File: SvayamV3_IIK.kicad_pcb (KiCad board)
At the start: 2 copper layers, 169 parts, among them J1 USB_C_Receptacle_USB2.0_16P, J10 POWER2, J11 TELEM1, J12 TELEM2, J13 GPS, J14 SERIAL4, J15 SERIAL5, J16 I2C, J17 CAN, J18 BUZZER, J19 Conn_01x05_Pin, J2 Micro_SD_Card_Det1, J20 ADC, J21 SPI, J22 SAFETY, J23 CAN2, J24 SBUS, J3 S_TOP_SIG, J4 S_TOP_PWR, J5 S_TOP_GND, J6 S_SIDE_SIG, J7 S_SIDE_PWR, J8 S_SIDE_GND, J9 POWER1, Q1 AO3400A, SW1 TS-1010A-B, SW2 SK-3296S-01-L3, U1 STM32H743IIKx, U10 RT9080-33GJ5, U11 AP22804AW5, U12 USBLC6-2SC6, U13 TJA1051TK-3, U2 TJA1051TK-3, U3 FM25CL64B, U4 BMI088, U5 BMI270, U6 BMP388, U7 BMM150, U8 TPS2120YFPR, U9 RT9080-33GJ5, Y1 X50328MSB2GI

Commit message: Layout
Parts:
- added C46: 100n, Capacitor_SMD:C_0402_1005Metric, F.Cu at (171.0, 81.0)
- added C47: 4u7, Capacitor_SMD:C_0603_1608Metric, F.Cu at (171.6, 73.8)
- added C48: 4u7, Capacitor_SMD:C_0603_1608Metric, F.Cu at (171.6, 76.3)
- added C49: 100n, Capacitor_SMD:C_0402_1005Metric, F.Cu at (171.0, 83.0)
- added C50: 100n, Capacitor_SMD:C_0402_1005Metric, F.Cu at (171.0, 85.0)
- added C51: 10u, Capacitor_SMD:C_0603_1608Metric, F.Cu at (171.6, 78.8)
- added D6: SMAJ6.0A, Diode_SMD:D_SMA, F.Cu at (165.6, 74.8)
- added D7: SMAJ6.0A, Diode_SMD:D_SMA, F.Cu at (165.6, 79.3)
- added R75: 100k, Resistor_SMD:R_0402_1005Metric, F.Cu at (163.0, 82.6)
- added R76: 100k, Resistor_SMD:R_0402_1005Metric, F.Cu at (163.0, 84.6)
- J10, J11, J12, J13, J14, J15, J16, J17, J18, J22, J3, J4, J5, J6, J7, J8, J9: moved to B.Cu
- U1: value STM32H743IIKx -> STM32H743IIK6
- moved H4 127.0 mm to (150.3, 101.2)
- moved H2 114.2 mm to (150.3, 38.3)
- moved J11 106.3 mm to (137.9, 42.6), turned to 180 degrees
- moved J13 106.0 mm to (139.0, 62.4), turned to 180 degrees
- moved J14 100.6 mm to (134.1, 72.5), turned to 180 degrees
- moved H3 95.7 mm to (107.3, 101.3)
- moved J12 93.8 mm to (121.4, 42.4), turned to 180 degrees
- moved J6 91.5 mm to (113.0, 95.5), turned to -90 degrees
- moved R28 89.4 mm to (142.0, 90.5)
- moved R41 89.0 mm to (135.9, 92.5), turned to -90 degrees
- moved R40 88.2 mm to (133.3, 92.5), turned to -90 degrees
- moved J15 87.8 mm to (118.1, 72.6), turned to 180 degrees
- moved R39 87.6 mm to (130.8, 92.5), turned to -90 degrees
- moved R38 87.0 mm to (128.2, 92.5), turned to -90 degrees
- moved R32 87.0 mm to (113.0, 92.4), turned to -90 degrees
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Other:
- board outline added: 51 x 70 mm
- copper layers 2 -> 6

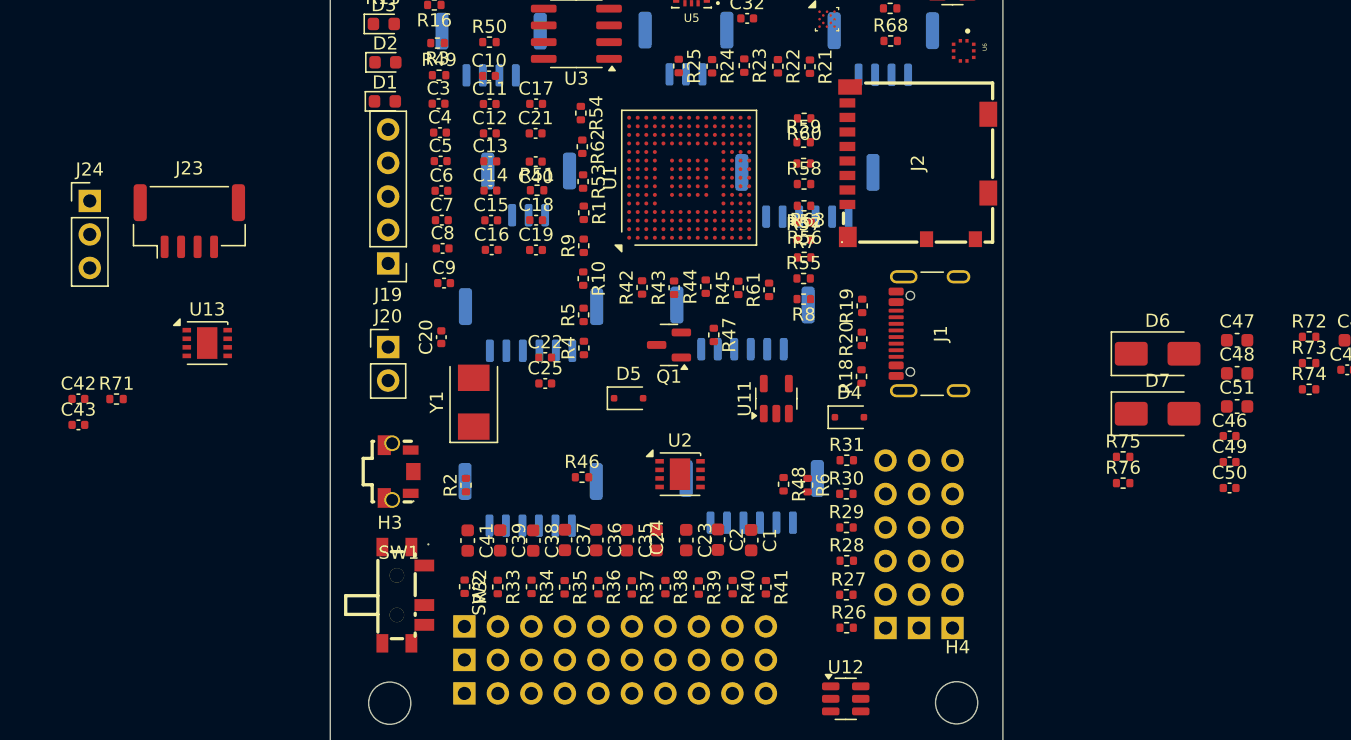
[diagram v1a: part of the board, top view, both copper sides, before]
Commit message: Schematic: sensor redundancy + blok current limiter GPS (terverifikasi)
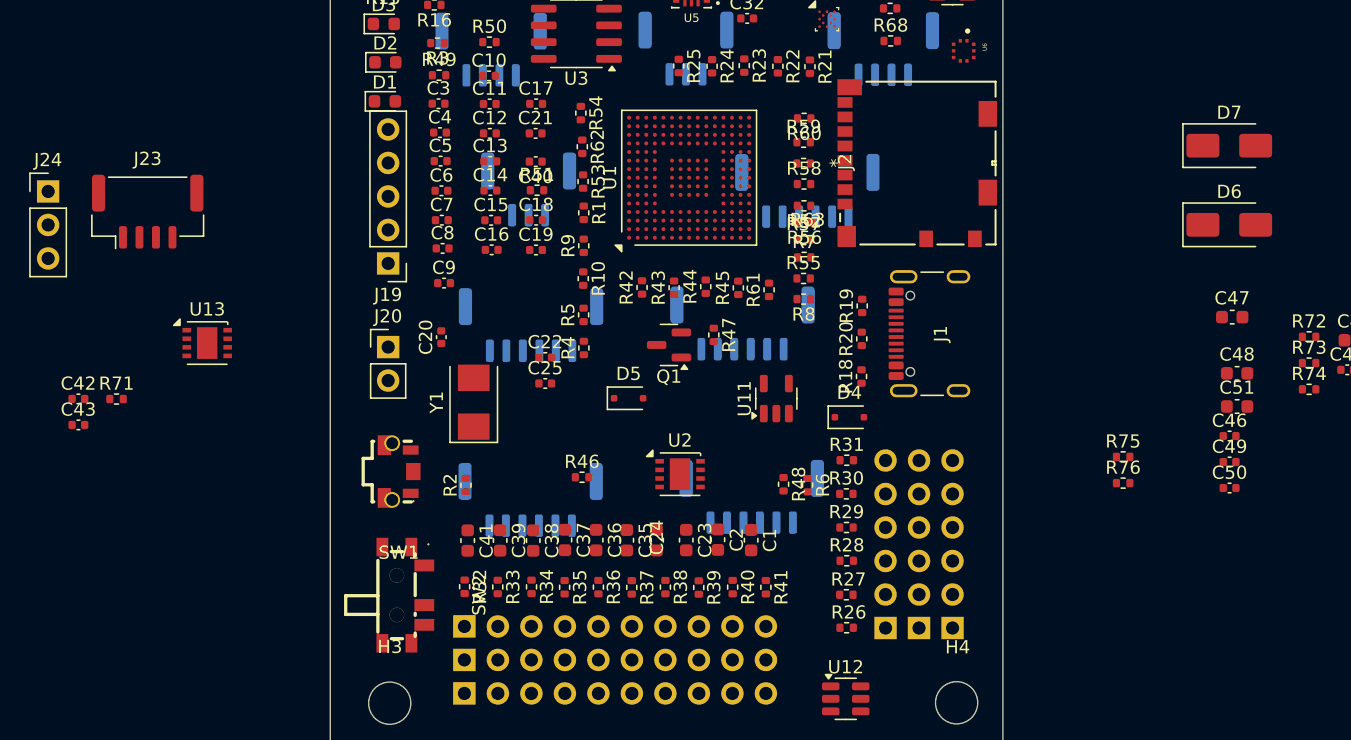
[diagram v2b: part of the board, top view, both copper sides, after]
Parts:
- J2: footprint easyeda2kicad:SIM-SMD_8P-1040310811 -> Svayam:104031-0811_MOL
- moved D7 21.0 mm to (171.0, 59.0)
- moved D6 11.2 mm to (171.0, 65.0)
- moved J23 3.24 mm to (89.0, 64.0)
- moved J24 3.24 mm to (81.5, 62.5)
- moved C47 1.79 mm to (171.2, 72.0)

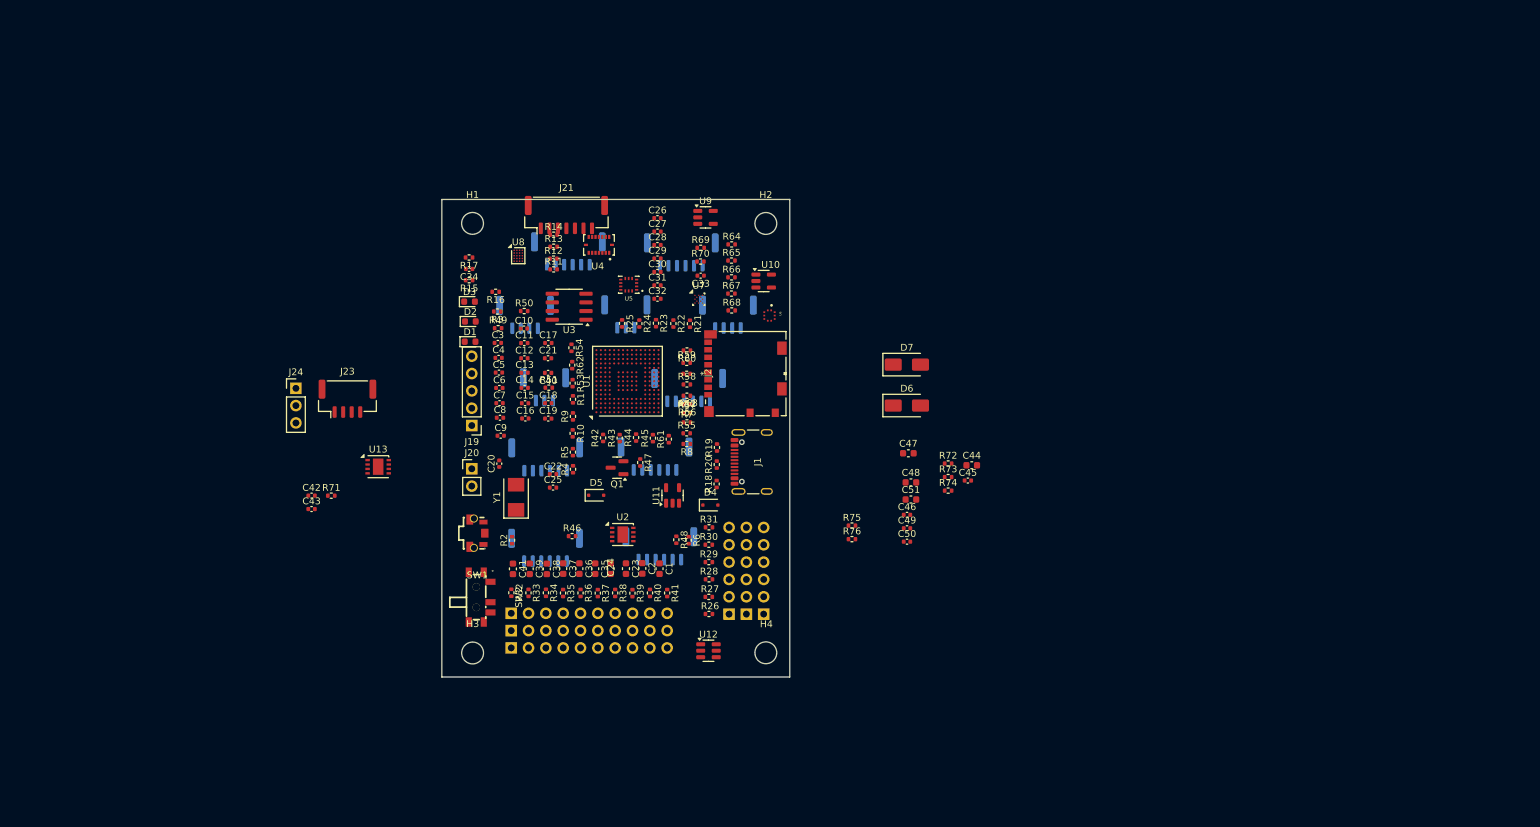
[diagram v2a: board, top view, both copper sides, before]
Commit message: PCB: F8 apply — 290 footprint di board (parity 0, verified)
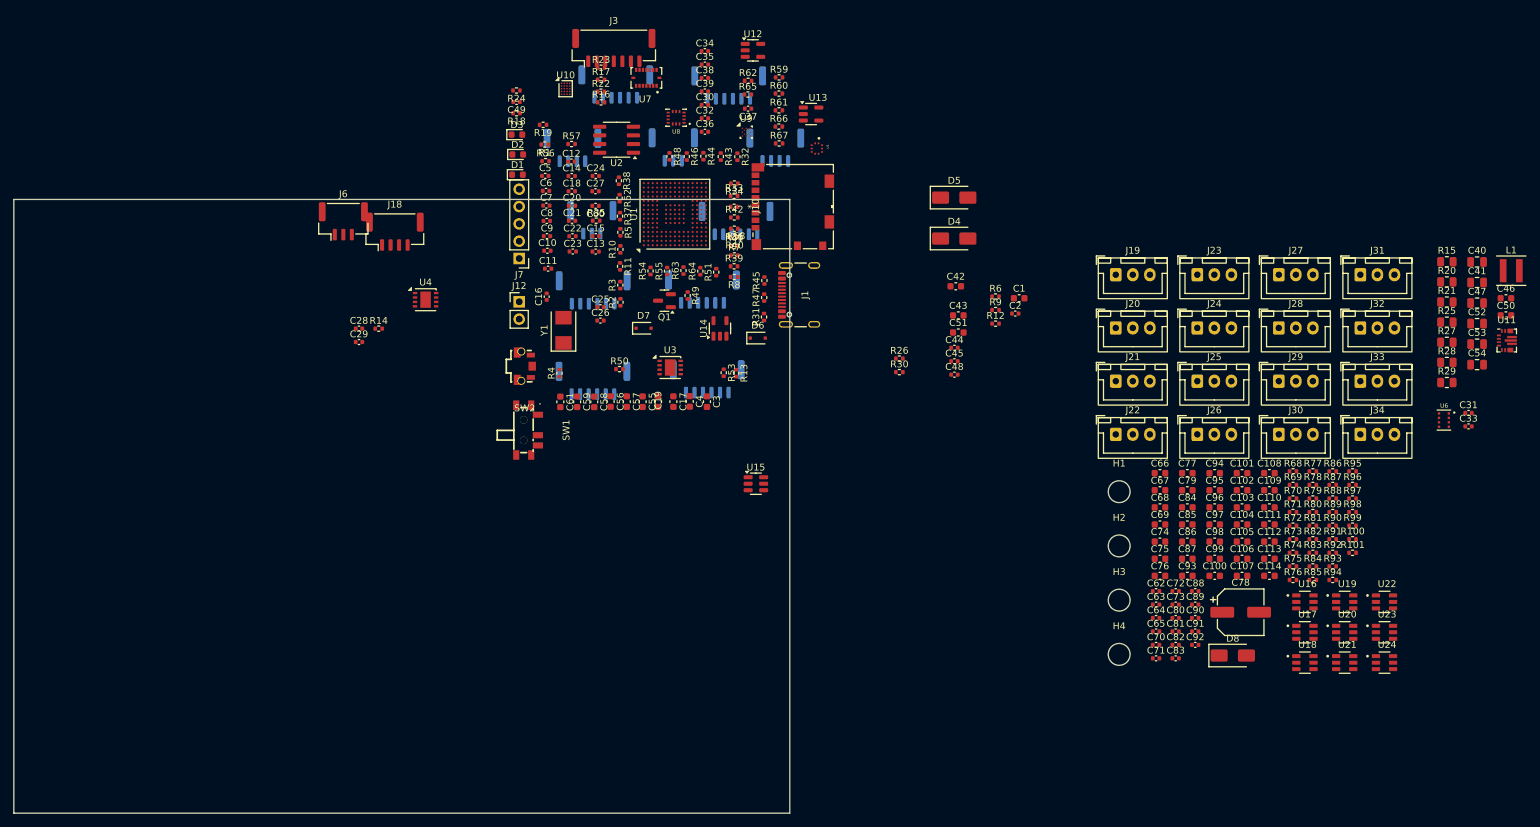
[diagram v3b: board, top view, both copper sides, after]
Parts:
- removed the J3 at (144.9, 95.6)
- removed the J4 at (147.5, 95.6)
- removed the J5 at (150.0, 95.6)
- removed the J6 at (113.0, 95.5)
- removed the J7 at (113.0, 98.0)
- removed the J8 at (113.0, 100.5)
- removed the R26 at (142.0, 95.5)
- removed the R30 at (142.0, 85.4)
- removed the R31 at (142.0, 82.8)
- removed the R32 at (113.0, 92.4)
- removed the R33 at (115.5, 92.5)
- removed the R34 at (118.1, 92.5)
- removed the R35 at (120.6, 92.5)
- removed the R36 at (123.2, 92.5)
- removed the R37 at (125.7, 92.5)
- removed the R38 at (128.2, 92.5)
- removed the R39 at (130.8, 92.5)
- removed the R40 at (133.3, 92.5)
- removed the R41 at (135.9, 92.5)
- added C100: 1u, Capacitor_SMD:C_0603_1608Metric, F.Cu at (216.1, 90.0)
- added C101: 1u, Capacitor_SMD:C_0603_1608Metric, F.Cu at (220.1, 74.9)
- added C102: 1u, Capacitor_SMD:C_0603_1608Metric, F.Cu at (220.1, 77.4)
- added C103: 1u, Capacitor_SMD:C_0603_1608Metric, F.Cu at (220.1, 79.9)
- added C104: 1u, Capacitor_SMD:C_0603_1608Metric, F.Cu at (220.1, 82.4)
- added C105: 1u, Capacitor_SMD:C_0603_1608Metric, F.Cu at (220.1, 84.9)
- added C106: 1u, Capacitor_SMD:C_0603_1608Metric, F.Cu at (220.1, 87.5)
- added C107: 1u, Capacitor_SMD:C_0603_1608Metric, F.Cu at (220.1, 90.0)
- added C108: 1u, Capacitor_SMD:C_0603_1608Metric, F.Cu at (224.1, 74.9)
- added C109: 1u, Capacitor_SMD:C_0603_1608Metric, F.Cu at (224.1, 77.4)
- added C110: 1u, Capacitor_SMD:C_0603_1608Metric, F.Cu at (224.1, 79.9)
- added C111: 1u, Capacitor_SMD:C_0603_1608Metric, F.Cu at (224.1, 82.4)
- added C112: 1u, Capacitor_SMD:C_0603_1608Metric, F.Cu at (224.1, 84.9)
- added C113: 1u, Capacitor_SMD:C_0603_1608Metric, F.Cu at (224.1, 87.5)
- added C114: 1u, Capacitor_SMD:C_0603_1608Metric, F.Cu at (224.1, 90.0)
- added C31: 100n, Capacitor_SMD:C_0402_1005Metric, F.Cu at (253.3, 66.1)
- added C33: 100n, Capacitor_SMD:C_0402_1005Metric, F.Cu at (253.3, 68.1)
- added C40: 10u, Capacitor_SMD:C_0805_2012Metric, F.Cu at (254.6, 44.0)
- added C41: 10u, Capacitor_SMD:C_0805_2012Metric, F.Cu at (254.6, 47.0)
- added C46: 10u, Capacitor_SMD:C_0603_1608Metric, F.Cu at (258.8, 49.3)
- added C47: 100n, Capacitor_SMD:C_0805_2012Metric, F.Cu at (254.6, 50.0)
- added C50: 10u, Capacitor_SMD:C_0603_1608Metric, F.Cu at (258.8, 51.8)
- added C52: 22u, Capacitor_SMD:C_0805_2012Metric, F.Cu at (254.6, 53.0)
- added C53: 22u, Capacitor_SMD:C_0805_2012Metric, F.Cu at (254.6, 56.0)
- added C54: 22u, Capacitor_SMD:C_0805_2012Metric, F.Cu at (254.6, 59.0)
- added C62: 100n, Capacitor_SMD:C_0402_1005Metric, F.Cu at (207.5, 92.2)
- added C63: 100n, Capacitor_SMD:C_0402_1005Metric, F.Cu at (207.5, 94.2)
- added C64: 100n, Capacitor_SMD:C_0402_1005Metric, F.Cu at (207.5, 96.1)
- added C65: 100n, Capacitor_SMD:C_0402_1005Metric, F.Cu at (207.5, 98.1)
- added C66: 1u, Capacitor_SMD:C_0603_1608Metric, F.Cu at (208.1, 74.9)
- added C67: 1u, Capacitor_SMD:C_0603_1608Metric, F.Cu at (208.1, 77.4)
- added C68: 1u, Capacitor_SMD:C_0603_1608Metric, F.Cu at (208.1, 79.9)
- added C69: 1u, Capacitor_SMD:C_0603_1608Metric, F.Cu at (208.1, 82.4)
- added C70: 100n, Capacitor_SMD:C_0402_1005Metric, F.Cu at (207.5, 100.1)
- added C71: 100n, Capacitor_SMD:C_0402_1005Metric, F.Cu at (207.5, 102.1)
- added C72: 100n, Capacitor_SMD:C_0402_1005Metric, F.Cu at (210.4, 92.2)
- added C73: 100n, Capacitor_SMD:C_0402_1005Metric, F.Cu at (210.4, 94.2)
- added C74: 1u, Capacitor_SMD:C_0603_1608Metric, F.Cu at (208.1, 84.9)
- added C75: 1u, Capacitor_SMD:C_0603_1608Metric, F.Cu at (208.1, 87.5)
- added C76: 1u, Capacitor_SMD:C_0603_1608Metric, F.Cu at (208.1, 90.0)
- added C77: 1u, Capacitor_SMD:C_0603_1608Metric, F.Cu at (212.1, 74.9)
- added C78: 220u, Capacitor_SMD:CP_Elec_6.3x7.7, F.Cu at (219.9, 95.3)
- added C79: 1u, Capacitor_SMD:C_0603_1608Metric, F.Cu at (212.1, 77.4)
- added C80: 100n, Capacitor_SMD:C_0402_1005Metric, F.Cu at (210.4, 96.1)
- added C81: 100n, Capacitor_SMD:C_0402_1005Metric, F.Cu at (210.4, 98.1)
- added C82: 100n, Capacitor_SMD:C_0402_1005Metric, F.Cu at (210.4, 100.1)
- added C83: 100n, Capacitor_SMD:C_0402_1005Metric, F.Cu at (210.4, 102.1)
- added C84: 1u, Capacitor_SMD:C_0603_1608Metric, F.Cu at (212.1, 79.9)
- added C85: 1u, Capacitor_SMD:C_0603_1608Metric, F.Cu at (212.1, 82.4)
- added C86: 1u, Capacitor_SMD:C_0603_1608Metric, F.Cu at (212.1, 84.9)
- added C87: 1u, Capacitor_SMD:C_0603_1608Metric, F.Cu at (212.1, 87.5)
- added C88: 100n, Capacitor_SMD:C_0402_1005Metric, F.Cu at (213.3, 92.2)
- added C89: 100n, Capacitor_SMD:C_0402_1005Metric, F.Cu at (213.3, 94.2)
- added C90: 100n, Capacitor_SMD:C_0402_1005Metric, F.Cu at (213.3, 96.1)
- added C91: 100n, Capacitor_SMD:C_0402_1005Metric, F.Cu at (213.3, 98.1)
- added C92: 100n, Capacitor_SMD:C_0402_1005Metric, F.Cu at (213.3, 100.1)
- added C93: 1u, Capacitor_SMD:C_0603_1608Metric, F.Cu at (212.1, 90.0)
- added C94: 1u, Capacitor_SMD:C_0603_1608Metric, F.Cu at (216.1, 74.9)
- added C95: 1u, Capacitor_SMD:C_0603_1608Metric, F.Cu at (216.1, 77.4)
- added C96: 1u, Capacitor_SMD:C_0603_1608Metric, F.Cu at (216.1, 79.9)
- added C97: 1u, Capacitor_SMD:C_0603_1608Metric, F.Cu at (216.1, 82.4)
- added C98: 1u, Capacitor_SMD:C_0603_1608Metric, F.Cu at (216.1, 84.9)
- added C99: 1u, Capacitor_SMD:C_0603_1608Metric, F.Cu at (216.1, 87.5)
- added D8: SMAJ6.0A, Diode_SMD:D_SMA, F.Cu at (218.8, 101.6)
- added J19: Channel 1, Connector_JST:JST_XH_B3B-XH-A_1x03_P2.50mm_Vertical, F.Cu at (201.6, 45.8)
- added J20: Channel 5, Connector_JST:JST_XH_B3B-XH-A_1x03_P2.50mm_Vertical, F.Cu at (201.6, 53.6)
- added J21: Channel 9, Connector_JST:JST_XH_B3B-XH-A_1x03_P2.50mm_Vertical, F.Cu at (201.6, 61.4)
- added J22: Channel 13, Connector_JST:JST_XH_B3B-XH-A_1x03_P2.50mm_Vertical, F.Cu at (201.6, 69.2)
- added J23: Channel 2, Connector_JST:JST_XH_B3B-XH-A_1x03_P2.50mm_Vertical, F.Cu at (213.6, 45.8)
- added J24: Channel 6, Connector_JST:JST_XH_B3B-XH-A_1x03_P2.50mm_Vertical, F.Cu at (213.6, 53.6)
- added J25: Channel 10, Connector_JST:JST_XH_B3B-XH-A_1x03_P2.50mm_Vertical, F.Cu at (213.6, 61.4)
- added J26: Channel 14, Connector_JST:JST_XH_B3B-XH-A_1x03_P2.50mm_Vertical, F.Cu at (213.6, 69.2)
- added J27: Channel 3, Connector_JST:JST_XH_B3B-XH-A_1x03_P2.50mm_Vertical, F.Cu at (225.5, 45.8)
- added J28: Channel 7, Connector_JST:JST_XH_B3B-XH-A_1x03_P2.50mm_Vertical, F.Cu at (225.5, 53.6)
- added J29: Channel 11, Connector_JST:JST_XH_B3B-XH-A_1x03_P2.50mm_Vertical, F.Cu at (225.5, 61.4)
- added J30: Channel 15, Connector_JST:JST_XH_B3B-XH-A_1x03_P2.50mm_Vertical, F.Cu at (225.5, 69.2)
- added J31: Channel 4, Connector_JST:JST_XH_B3B-XH-A_1x03_P2.50mm_Vertical, F.Cu at (237.5, 45.8)
- added J32: Channel 8, Connector_JST:JST_XH_B3B-XH-A_1x03_P2.50mm_Vertical, F.Cu at (237.5, 53.6)
- added J33: Channel 12, Connector_JST:JST_XH_B3B-XH-A_1x03_P2.50mm_Vertical, F.Cu at (237.5, 61.4)
- added J34: Channel 16, Connector_JST:JST_XH_B3B-XH-A_1x03_P2.50mm_Vertical, F.Cu at (237.5, 69.2)
- added L1: 1.5u, Svayam:L_Coilcraft_XxL4020, F.Cu at (259.6, 45.2)
- added R100: 10k, Resistor_SMD:R_0402_1005Metric, F.Cu at (236.3, 84.6)
- added R101: 10k, Resistor_SMD:R_0402_1005Metric, F.Cu at (236.3, 86.6)
- added R15: 10k, Resistor_SMD:R_0805_2012Metric, F.Cu at (250.2, 43.9)
- added R20: 100k, Resistor_SMD:R_0805_2012Metric, F.Cu at (250.2, 46.9)
- added R21: 10k, Resistor_SMD:R_0805_2012Metric, F.Cu at (250.2, 49.8)
- added R25: 100k, Resistor_SMD:R_0805_2012Metric, F.Cu at (250.2, 52.8)
- added R68: 120, Resistor_SMD:R_0402_1005Metric, F.Cu at (227.6, 74.6)
- added R69: 120, Resistor_SMD:R_0402_1005Metric, F.Cu at (227.6, 76.6)
- added R70: 120, Resistor_SMD:R_0402_1005Metric, F.Cu at (227.6, 78.6)
- added R71: 120, Resistor_SMD:R_0402_1005Metric, F.Cu at (227.6, 80.6)
- added R72: 120, Resistor_SMD:R_0402_1005Metric, F.Cu at (227.6, 82.6)
- added R73: 120, Resistor_SMD:R_0402_1005Metric, F.Cu at (227.6, 84.6)
- added R74: 120, Resistor_SMD:R_0402_1005Metric, F.Cu at (227.6, 86.6)
- added R75: 120, Resistor_SMD:R_0402_1005Metric, F.Cu at (227.6, 88.6)
- added R76: 120, Resistor_SMD:R_0402_1005Metric, F.Cu at (227.6, 90.6)
- added R77: 120, Resistor_SMD:R_0402_1005Metric, F.Cu at (230.5, 74.6)
- added R78: 120, Resistor_SMD:R_0402_1005Metric, F.Cu at (230.5, 76.6)
- added R79: 120, Resistor_SMD:R_0402_1005Metric, F.Cu at (230.5, 78.6)
- added R80: 120, Resistor_SMD:R_0402_1005Metric, F.Cu at (230.5, 80.6)
- added R81: 120, Resistor_SMD:R_0402_1005Metric, F.Cu at (230.5, 82.6)
- added R82: 120, Resistor_SMD:R_0402_1005Metric, F.Cu at (230.5, 84.6)
- added R83: 120, Resistor_SMD:R_0402_1005Metric, F.Cu at (230.5, 86.6)
- added R84: 33k, Resistor_SMD:R_0402_1005Metric, F.Cu at (230.5, 88.6)
- added R85: 33k, Resistor_SMD:R_0402_1005Metric, F.Cu at (230.5, 90.6)
- added R86: 75k, Resistor_SMD:R_0402_1005Metric, F.Cu at (233.4, 74.6)
- added R87: 75k, Resistor_SMD:R_0402_1005Metric, F.Cu at (233.4, 76.6)
- added R88: 110k, Resistor_SMD:R_0402_1005Metric, F.Cu at (233.4, 78.6)
- added R89: 47k, Resistor_SMD:R_0402_1005Metric, F.Cu at (233.4, 80.6)
- added R90: 56k, Resistor_SMD:R_0402_1005Metric, F.Cu at (233.4, 82.6)
- added R91: 110k, Resistor_SMD:R_0402_1005Metric, F.Cu at (233.4, 84.6)
- added R92: 47k, Resistor_SMD:R_0402_1005Metric, F.Cu at (233.4, 86.6)
- added R93: 10k, Resistor_SMD:R_0402_1005Metric, F.Cu at (233.4, 88.6)
- added R94: 10k, Resistor_SMD:R_0402_1005Metric, F.Cu at (233.4, 90.6)
- added R95: 10k, Resistor_SMD:R_0402_1005Metric, F.Cu at (236.3, 74.6)
- added R96: 10k, Resistor_SMD:R_0402_1005Metric, F.Cu at (236.3, 76.6)
- added R97: 10k, Resistor_SMD:R_0402_1005Metric, F.Cu at (236.3, 78.6)
- added R98: 10k, Resistor_SMD:R_0402_1005Metric, F.Cu at (236.3, 80.6)
- added R99: 10k, Resistor_SMD:R_0402_1005Metric, F.Cu at (236.3, 82.6)
- added U11: TPS63070, Svayam:VQFN-HR-15, F.Cu at (258.9, 55.5)
- added U16: TPS2553DBVT, Svayam:SOT95P280X145-6N, F.Cu at (229.3, 93.8)
- added U17: TPS2553DBVT, Svayam:SOT95P280X145-6N, F.Cu at (229.3, 98.2)
- added U18: TPS2553DBVT, Svayam:SOT95P280X145-6N, F.Cu at (229.3, 102.7)
- added U19: TPS2553DBVT, Svayam:SOT95P280X145-6N, F.Cu at (235.2, 93.8)
- added U20: TPS2553DBVT, Svayam:SOT95P280X145-6N, F.Cu at (235.2, 98.2)
- added U21: TPS2553DBVT, Svayam:SOT95P280X145-6N, F.Cu at (235.2, 102.7)
- added U22: TPS2553DBVT, Svayam:SOT95P280X145-6N, F.Cu at (241.0, 93.8)
- added U23: TPS2553DBVT, Svayam:SOT95P280X145-6N, F.Cu at (241.0, 98.2)
- added U24: TPS2553DBVT, Svayam:SOT95P280X145-6N, F.Cu at (241.0, 102.7)
- added U6: DPS310XTSA1, Svayam:XDCR_DPS310XTSA1, F.Cu at (249.7, 67.1)
- H1, H2, H3, H4: value MountingHole_Pad -> MountingHole
- J6: renamed from J24; footprint Connector_PinHeader_2.54mm:PinHeader_1x03_P2.54mm_Vertical -> Connector_JST:JST_GH_BM03B-GHS-TBT_1x03-1MP_P1.25mm_Vertical
- R27: value 120 -> 68k; footprint Resistor_SMD:R_0402_1005Metric -> Resistor_SMD:R_0805_2012Metric
- R28: value 120 -> 13k; footprint Resistor_SMD:R_0402_1005Metric -> Resistor_SMD:R_0805_2012Metric
- R29: value 120 -> 100k; footprint Resistor_SMD:R_0402_1005Metric -> Resistor_SMD:R_0805_2012Metric
- moved R27 114.4 mm to (250.2, 55.7)
- moved R28 112.7 mm to (250.2, 58.7)
- moved R29 111.3 mm to (250.2, 61.6)
- moved H1 102.6 mm to (202.1, 77.6)
- moved H3 95.1 mm to (202.1, 93.5)
- moved H2 70.1 mm to (202.1, 85.6)
- moved H4 51.8 mm to (202.1, 101.5)
- moved C2 25.4 mm to (186.9, 51.5)
- moved C32 25.4 mm to (141.4, 22.9)
- moved C4 25.4 mm to (139.2, 64.4)
- moved C55 25.4 mm to (132.3, 64.4)
- moved D6 25.4 mm to (149.2, 55.1)
- moved R2 25.4 mm to (129.0, 49.9)
- moved R33 25.4 mm to (145.7, 34.3)
- moved R36 25.4 mm to (145.7, 39.1)
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- renumbered C44 to C1, C8 to C10, C9 to C11, C10 to C12, C19 to C13, C11 to C14, C18 to C15, C20 to C16, C23 to C17, C12 to C18, C24 to C19, C45 to C2, C13 to C20, C14 to C21, C15 to C22, C16 to C23, C17 to C24, C22 to C25, C25 to C26, C21 to C27, C42 to C28, C43 to C29, C1 to C3, C31 to C32, C26 to C34, C27 to C35, C32 to C36, C33 to C37, C28 to C38, C29 to C39, C2 to C4, C47 to C42, C48 to C43, C46 to C44, C49 to C45, C50 to C48, C34 to C49, C3 to C5, C35 to C55, C37 to C56, C36 to C57, C38 to C58, C39 to C59, C4 to C6, C40 to C60, C41 to C61, C5 to C7, C6 to C8, C7 to C9, D6 to D4, D7 to D5, D4 to D6, D5 to D7, J2 to J10, J18 to J11, J20 to J12, J17 to J13, J15 to J14, J22 to J15, J10 to J16, J16 to J17, J23 to J18, J13 to J2, J21 to J3, J11 to J4, J12 to J5, J19 to J7, J14 to J8, R3 to R1, R9 to R10, R10 to R11, R74 to R12, R6 to R13, R71 to R14, R11 to R16, R13 to R17, R15 to R18, R16 to R19, R4 to R2, R12 to R22, R14 to R23, R17 to R24, R75 to R26, R5 to R3, R76 to R30, R18 to R31, R21 to R32, R59 to R33, R60 to R34, R51 to R35, R52 to R36, R53 to R37, R54 to R38, R55 to R39, R2 to R4, R56 to R40, R57 to R41, R58 to R42, R22 to R43, R23 to R44, R19 to R45, R24 to R46, R20 to R47, R25 to R48, R47 to R49, R1 to R5, R46 to R50, R61 to R51, R62 to R52, R48 to R53, R42 to R54, R43 to R55, R49 to R56, R50 to R57, R63 to R58, R64 to R59, R72 to R6, R65 to R60, R66 to R61, R69 to R62, R44 to R63, R45 to R64, R70 to R65, R67 to R66, R68 to R67, R73 to R9, SW2 to SW1, SW1 to SW2, U8 to U10, U9 to U12, U10 to U13, U11 to U14, U12 to U15, U3 to U2, U2 to U3, U13 to U4, U6 to U5, U4 to U7, U5 to U8, U7 to U9
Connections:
- C48 pad 1: +5V_IN -> /Power/VIN_BB
- C51 pad 1: +5V_IN -> /Power/VIN_BB
- D6 pad 1: +5V_IN -> /Power/VIN_BB
- J13 pad 1: +5V_PERIPH -> +5V_CAN
- J14 pad 1: +5V_PERIPH -> +5V_SERIAL5
- J17 pad 1: +5V_PERIPH -> +5V_I2C
- J18 pad 1: +5V_PERIPH -> +5V_CAN2
- J2 pad 1: +5V_PERIPH -> +5V_GPS
- J3 pad 1: +5V_PERIPH -> +5V_SPI
- J4 pad 1: +5V_PERIPH -> +5V_TELEM1
- J5 pad 1: +5V_PERIPH -> +5V_TELEM2
- J8 pad 1: +5V_PERIPH -> +5V_SERIAL4
- R27 pad 1: TIM1_CH3 -> +5V_IN
- R27 pad 2: Net-(J3-Pin_2) -> /Power/FB
- R28 pad 1: TIM1_CH2 -> /Power/FB
- R28 pad 2: Net-(J3-Pin_3) -> GND
- R29 pad 1: TIM1_CH1 -> +5V_IN
- U1 pad B12: unconnected-(U1-PD0-PadB12) -> ~{GPS_OC}
- U1 pad C12: unconnected-(U1-PD1-PadC12) -> ~{TELEM1_OC}
- U1 pad C13: unconnected-(U1-PI3-PadC13) -> BARO2_SPI2_MOSI
- U1 pad D14: unconnected-(U1-PI1-PadD14) -> BARO2_SPI2_SCK
- U1 pad E14: unconnected-(U1-PI0-PadE14) -> ~{BARO2_CS_N}
- U1 pad M4: unconnected-(U1-PC2_C-PadM4) -> BARO2_SPI2_MISO
- U1 pad N11: unconnected-(U1-PE13-PadN11) -> ~{CAN_OC}
- U1 pad P10: unconnected-(U1-PE11-PadP10) -> ~{SERIAL5_OC}
- U1 pad P11: unconnected-(U1-PE14-PadP11) -> ~{CAN2_OC}
- U1 pad P14: unconnected-(U1-PD9-PadP14) -> ~{SERIAL4_OC}
- U1 pad P15: unconnected-(U1-PD8-PadP15) -> ~{TELEM2_OC}
- U1 pad R10: unconnected-(U1-PE12-PadR10) -> ~{I2C_OC}
- U1 pad R11: unconnected-(U1-PE15-PadR11) -> ~{SPI_OC}
- U1 pad R2: unconnected-(U1-PA3-PadR2) -> ~{PERI_OC}
- U10 pad C2: +5V_IN -> /Power/VIN_BB
- U10 pad C3: +5V_IN -> /Power/VIN_BB
- U10 pad D1: +5V_IN -> /Power/VIN_BB
- U10 pad D2: +5V_IN -> /Power/VIN_BB
- U10 pad D3: +5V_IN -> /Power/VIN_BB
- U10 pad D4: +5V_IN -> /Power/VIN_BB
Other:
- board size 51 x 70 mm -> 113.7 x 90 mm

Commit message: PCB: placement dimulai — re-arrange komponen oleh user (checkpoint)
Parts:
- moved C16 22.2 mm to (139.9, 54.1)
- moved C61 22.2 mm to (141.9, 69.5)
- moved C1 22.2 mm to (209.1, 54.3)
- moved C10 22.2 mm to (140.0, 47.4)
- moved C100 22.2 mm to (237.8, 95.0)
- moved C101 22.2 mm to (241.8, 80.0)
- moved C102 22.2 mm to (241.8, 82.5)
- moved C103 22.2 mm to (241.8, 85.0)
- moved C104 22.2 mm to (241.8, 87.5)
- moved C105 22.2 mm to (241.8, 90.0)
- moved C106 22.2 mm to (241.8, 92.5)
- moved C107 22.2 mm to (241.8, 95.0)
- moved C14 22.2 mm to (143.5, 36.4)
- moved C15 22.2 mm to (147.1, 45.2)
- moved C17 22.2 mm to (158.4, 69.5)
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
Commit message: checkpoint: remap label TIM + swap silk servo (pre-F8)
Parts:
- J1, J18, J3, J6, R31, R45, R47: moved to B.Cu
- moved R70 227.9 mm to (40.1, 174.2), turned to -90 degrees
- moved R68 223.7 mm to (40.1, 159.2), turned to -90 degrees
- moved J19 215.3 mm to (40.1, 164.2)
- moved J23 214.9 mm to (52.6, 164.2)
- moved J21 214.7 mm to (40.1, 178.6)
- moved J27 214.5 mm to (65.0, 164.2)
- moved J25 214.3 mm to (52.6, 178.6)
- moved J31 214.1 mm to (77.4, 164.2)
- moved J29 213.9 mm to (65.0, 178.6)
- moved J33 213.5 mm to (77.4, 178.6)
- moved R74 213.2 mm to (52.6, 174.0), turned to -90 degrees
- moved R72 209.6 mm to (52.2, 159.2), turned to -90 degrees
- moved R78 208.7 mm to (65.0, 173.9), turned to -90 degrees
- moved C64 203.6 mm to (39.1, 174.2), turned to -90 degrees
- moved C62 199.9 mm to (39.1, 159.2), turned to -90 degrees
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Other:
- board size 113.7 x 90 mm -> 131.4 x 90 mm

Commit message: PCB checkpoint sebelum F8 (setelah swap label TIM4 connector)
290 footprint, 1412 segmen track, 312 via, 185 net sudah ada copper.
Titik rollback sebelum Update PCB from Schematic (swap TIM4_CH2/CH3).
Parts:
- C1, C10, C11, C12, C14, C17, C18, C19, C2, C20, C21, C22, C23, C24, C28, C3, C4, C48, C5, C51, C6, C62, C63, C64, C65, C66, C67, C68, C69, C7, C70, C71, C72, C73, C74, C75, C76, C77, C8, C80, C81, C82, C83, C84, C85, C86, C87, C89, C9, C90, C91, C92, C93, C94, C95, C96, D6, R10, R11, R33, R35, R37, R39, R41, R5, R51, R56, R58, R60, R62, R65, R66, R67, R84, R85, R86, R87, R88, R89, R90, R91, R92, U15: moved to B.Cu
- J6, R31: moved to F.Cu
- moved D4 241.5 mm to (54.8, 132.9), turned to -90 degrees
- moved C47 235.2 mm to (59.0, 145.3), turned to 90 degrees
- moved C42 234.4 mm to (58.3, 130.8), turned to -90 degrees
- moved R25 234.1 mm to (55.1, 146.3)
- moved U11 233.7 mm to (62.0, 143.1)
- moved C50 233.3 mm to (64.4, 144.8), turned to 90 degrees
- moved C46 232.9 mm to (64.4, 141.3), turned to -90 degrees
- moved C40 232.9 mm to (61.9, 139.9), turned to 180 degrees
- moved L1 232.0 mm to (68.7, 143.1), turned to -90 degrees
- moved C52 231.9 mm to (61.8, 146.2), turned to 180 degrees
- moved D5 231.7 mm to (68.5, 131.5), turned to -90 degrees
- moved R27 231.6 mm to (54.8, 141.6), turned to -90 degrees
- moved C44 231.4 mm to (57.1, 130.5), turned to -90 degrees
- moved R15 230.7 mm to (59.0, 137.9)
- moved C51 230.5 mm to (59.5, 130.2), turned to 180 degrees
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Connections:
- R68 pad 1: TIM8_CH4 -> TIM2_CH2
- R69 pad 1: TIM8_CH2 -> TIM3_CH4
- R70 pad 1: TIM5_CH1 -> TIM5_CH2
- R71 pad 1: TIM2_CH1 -> TIM1_CH1
- R72 pad 1: TIM1_CH3 -> TIM2_CH3
- R73 pad 1: TIM8_CH1 -> TIM3_CH3
- R74 pad 1: TIM5_CH2 -> TIM5_CH1
- R75 pad 1: TIM3_CH2 -> TIM1_CH2
- R76 pad 1: TIM1_CH2 -> TIM2_CH1
- R77 pad 1: TIM4_CH2 -> TIM4_CH3
- R78 pad 1: TIM3_CH3 -> TIM8_CH1
- R79 pad 1: TIM2_CH2 -> TIM1_CH3
- R80 pad 1: TIM1_CH1 -> TIM3_CH2
- R81 pad 1: TIM4_CH3 -> TIM4_CH2
- R82 pad 1: TIM3_CH4 -> TIM8_CH2
- R83 pad 1: TIM2_CH3 -> TIM8_CH4
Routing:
- net GND: track 0.00 -> 216.0 mm, vias 0 -> 107
- net +5V_PERIPH: track 0.00 -> 75.3 mm, vias 0 -> 24
- net TIM2_CH2: track 0.00 -> 66.6 mm
- net +VSERVO: track 0.00 -> 53.0 mm, vias 0 -> 14
- net TIM2_CH3: track 0.00 -> 52.7 mm
- net +3V3_FMU: track 0.00 -> 49.1 mm, vias 0 -> 21
- net TIM3_CH4: track 0.00 -> 42.1 mm
- net +5V_IN: track 0.00 -> 42.0 mm, vias 0 -> 10
- net TIM2_CH1: track 0.00 -> 41.4 mm, vias 0 -> 2
- net TIM3_CH3: track 0.00 -> 40.6 mm, vias 0 -> 1
- net /Power/VIN_BB: track 0.00 -> 33.9 mm, vias 0 -> 6
- net TIM3_CH2: track 0.00 -> 32.3 mm
- net +3V3_SENS: track 0.00 -> 31.7 mm, vias 0 -> 10
- net Net-(U1-PE6): track 0.00 -> 20.6 mm
- net Net-(U1-PE2): track 0.00 -> 18.1 mm
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- added copper zone on F.Cu, net +3V3_SENS
- added copper zone on F.Cu, net +5V_IN
- added copper zone on B.Cu, net +VSERVO
- added copper zone on F.Cu, net +VSERVO
- added copper zone on F.Cu, net /Power/VIN_BB
- added copper zone on B.Cu, net Net-(U11-L1)
- added copper zone on B.Cu, net Net-(U11-L2)
